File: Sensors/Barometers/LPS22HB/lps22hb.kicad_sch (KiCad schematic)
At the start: 2 parts

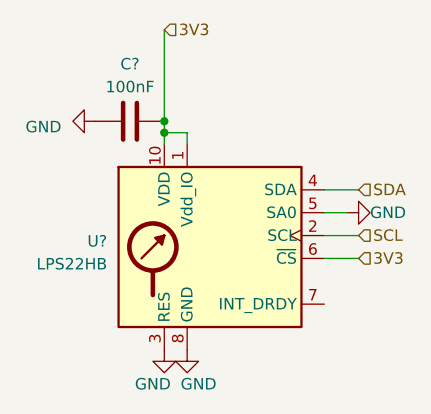
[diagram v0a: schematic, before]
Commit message: Added 18v-5v regulator circuit
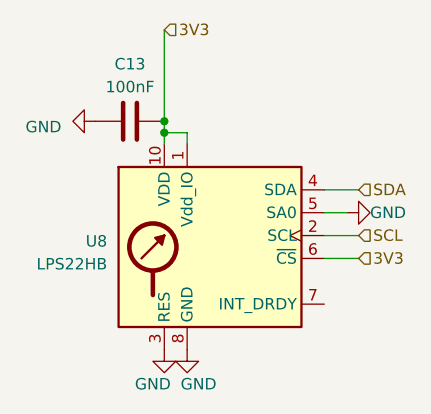
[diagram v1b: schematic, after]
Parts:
- gave numbers to parts that had none: 2
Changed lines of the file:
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@@
   (symbol (lib_id "power:GND") (at 134.62 81.28 270) (unit 1)
     (in_bom yes) (on_board yes) (dnp no) (fields_autoplaced)
-    (property "Reference" "#PWR?" (at 128.27 81.28 0)
+    (property "Reference" "#PWR050" (at 128.27 81.28 0)
       (effects (font (size 1.27 1.27)) hide)
     )
@@
     (pin "1")
     (instances
-      (project "skydiving-altimeter"
-        (path "/e63e39d7-6ac0-4ffd-8aa3-1841a4541b55/25087f50-b4bd-4ba8-9294-4cb0f29516ca"
-          (reference "#PWR?") (unit 1)
+      (project "avc-computer"
+        (path "/e63e39d7-6ac0-4ffd-8aa3-1841a4541b55/0097ce40-7767-41a4-a694-1129b95a764c/e9b8be52-4926-4d81-8d1e-4fa7fd6aec68"
+          (reference "#PWR050") (unit 1)
         )
       )
       (project "test"
         (path "/fdf4640f-6031-4faf-a4c3-82c41668722e/cf3ff100-abac-439e-b69e-f80961e3457f"
-          (reference "#PWR01") (unit 1)
+          (reference "#PWR?") (unit 1)
         )
       )
@@
   (symbol (lib_id "power:GND") (at 162.56 91.44 90) (unit 1)
     (in_bom yes) (on_board yes) (dnp no)
-    (property "Reference" "#PWR?" (at 168.91 91.44 0)
+    (property "Reference" "#PWR053" (at 168.91 91.44 0)
       (effects (font (size 1.27 1.27)) hide)
     )
@@
     (pin "1")
     (instances
-      (project "skydiving-altimeter"
-        (path "/e63e39d7-6ac0-4ffd-8aa3-1841a4541b55/25087f50-b4bd-4ba8-9294-4cb0f29516ca"
-          (reference "#PWR?") (unit 1)
+      (project "avc-computer"
+        (path "/e63e39d7-6ac0-4ffd-8aa3-1841a4541b55/0097ce40-7767-41a4-a694-1129b95a764c/e9b8be52-4926-4d81-8d1e-4fa7fd6aec68"
+          (reference "#PWR053") (unit 1)
         )
       )
       (project "test"
         (path "/fdf4640f-6031-4faf-a4c3-82c41668722e/cf3ff100-abac-439e-b69e-f80961e3457f"
-          (reference "#PWR04") (unit 1)
+          (reference "#PWR?") (unit 1)
         )
       )
@@
   (symbol (lib_id "Sensor_Pressure:LPS22HB") (at 147.32 96.52 0) (unit 1)
     (in_bom yes) (on_board yes) (dnp no) (fields_autoplaced)
-    (property "Reference" "U?" (at 135.89 94.615 0)
+    (property "Reference" "U8" (at 135.89 94.615 0)
       (effects (font (size 1.27 1.27)) (justify right))
     )
@@
     (pin "9")
     (instances
-      (project "skydiving-altimeter"
-        (path "/e63e39d7-6ac0-4ffd-8aa3-1841a4541b55/25087f50-b4bd-4ba8-9294-4cb0f29516ca"
-          (reference "U?") (unit 1)
+      (project "avc-computer"
+        (path "/e63e39d7-6ac0-4ffd-8aa3-1841a4541b55/0097ce40-7767-41a4-a694-1129b95a764c/e9b8be52-4926-4d81-8d1e-4fa7fd6aec68"
+          (reference "U8") (unit 1)
         )
       )
       (project "test"
         (path "/fdf4640f-6031-4faf-a4c3-82c41668722e/cf3ff100-abac-439e-b69e-f80961e3457f"
-          (reference "U1") (unit 1)
+          (reference "U?") (unit 1)
         )
       )
@@
   (symbol (lib_id "Device:C") (at 138.43 81.28 270) (unit 1)
     (in_bom yes) (on_board yes) (dnp no) (fields_autoplaced)
-    (property "Reference" "C?" (at 138.43 74.93 90)
+    (property "Reference" "C13" (at 138.43 74.93 90)
       (effects (font (size 1.27 1.27)))
     )
@@
     (pin "2")
     (instances
-      (project "skydiving-altimeter"
-        (path "/e63e39d7-6ac0-4ffd-8aa3-1841a4541b55/25087f50-b4bd-4ba8-9294-4cb0f29516ca"
-          (reference "C?") (unit 1)
+      (project "avc-computer"
+        (path "/e63e39d7-6ac0-4ffd-8aa3-1841a4541b55/0097ce40-7767-41a4-a694-1129b95a764c/e9b8be52-4926-4d81-8d1e-4fa7fd6aec68"
+          (reference "C13") (unit 1)
         )
       )
       (project "test"
         (path "/fdf4640f-6031-4faf-a4c3-82c41668722e/cf3ff100-abac-439e-b69e-f80961e3457f"
-          (reference "C1") (unit 1)
+          (reference "C?") (unit 1)
         )
       )
@@
   (symbol (lib_id "power:GND") (at 142.24 106.68 0) (unit 1)
     (in_bom yes) (on_board yes) (dnp no)
-    (property "Reference" "#PWR?" (at 142.24 113.03 0)
+    (property "Reference" "#PWR051" (at 142.24 113.03 0)
       (effects (font (size 1.27 1.27)) hide)
     )
@@
     (pin "1")
     (instances
-      (project "skydiving-altimeter"
-        (path "/e63e39d7-6ac0-4ffd-8aa3-1841a4541b55/25087f50-b4bd-4ba8-9294-4cb0f29516ca"
-          (reference "#PWR?") (unit 1)
+      (project "avc-computer"
+        (path "/e63e39d7-6ac0-4ffd-8aa3-1841a4541b55/0097ce40-7767-41a4-a694-1129b95a764c/e9b8be52-4926-4d81-8d1e-4fa7fd6aec68"
+          (reference "#PWR051") (unit 1)
         )
       )
       (project "test"
         (path "/fdf4640f-6031-4faf-a4c3-82c41668722e/cf3ff100-abac-439e-b69e-f80961e3457f"
-          (reference "#PWR02") (unit 1)
+          (reference "#PWR?") (unit 1)
         )
       )
@@
   (symbol (lib_id "power:GND") (at 144.78 106.68 0) (unit 1)
     (in_bom yes) (on_board yes) (dnp no)
-    (property "Reference" "#PWR?" (at 144.78 113.03 0)
+    (property "Reference" "#PWR052" (at 144.78 113.03 0)
       (effects (font (size 1.27 1.27)) hide)
     )
@@
     (pin "1")
     (instances
-      (project "skydiving-altimeter"
-        (path "/e63e39d7-6ac0-4ffd-8aa3-1841a4541b55/25087f50-b4bd-4ba8-9294-4cb0f29516ca"
-          (reference "#PWR?") (unit 1)
+      (project "avc-computer"
+        (path "/e63e39d7-6ac0-4ffd-8aa3-1841a4541b55/0097ce40-7767-41a4-a694-1129b95a764c/e9b8be52-4926-4d81-8d1e-4fa7fd6aec68"
+          (reference "#PWR052") (unit 1)
         )
       )
       (project "test"
         (path "/fdf4640f-6031-4faf-a4c3-82c41668722e/cf3ff100-abac-439e-b69e-f80961e3457f"
-          (reference "#PWR03") (unit 1)
+          (reference "#PWR?") (unit 1)
         )
       )
